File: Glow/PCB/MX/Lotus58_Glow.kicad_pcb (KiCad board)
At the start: 2 copper layers, 139.1 x 107.7 mm, 122 parts, among them J1 PJ-320A, P4 OLED, SW1 Kailh hotswap MX socket, SW10 Kailh hotswap MX socket, SW11 Kailh hotswap MX socket, SW12 Kailh hotswap MX socket, SW13 Kailh hotswap MX socket, SW14 Kailh hotswap MX socket, SW15 Kailh hotswap MX socket, SW16 Kailh hotswap MX socket, SW17 Kailh hotswap MX socket, SW18 Kailh hotswap MX socket, SW19 Kailh hotswap MX socket, SW2 Kailh hotswap MX socket, SW20 Kailh hotswap MX socket, SW21 Kailh hotswap MX socket, SW22 Kailh hotswap MX socket, SW23 Kailh hotswap MX socket, SW24 Kailh hotswap MX socket, SW25 Kailh hotswap MX socket, SW26 Kailh hotswap MX socket, SW27 Kailh hotswap MX socket, SW28 Kailh hotswap MX socket, SW29 Kailh hotswap MX socket, SW3 Kailh hotswap MX socket, SW30 Rotary_Encoder_Switch, SW31 Rotary_Encoder_Switch, SW4 Kailh hotswap MX socket, SW5 Kailh hotswap MX socket, SW6 Kailh hotswap MX socket, SW7 Kailh hotswap MX socket, SW8 Kailh hotswap MX socket, SW9 Kailh hotswap MX socket, U1 ProMicro

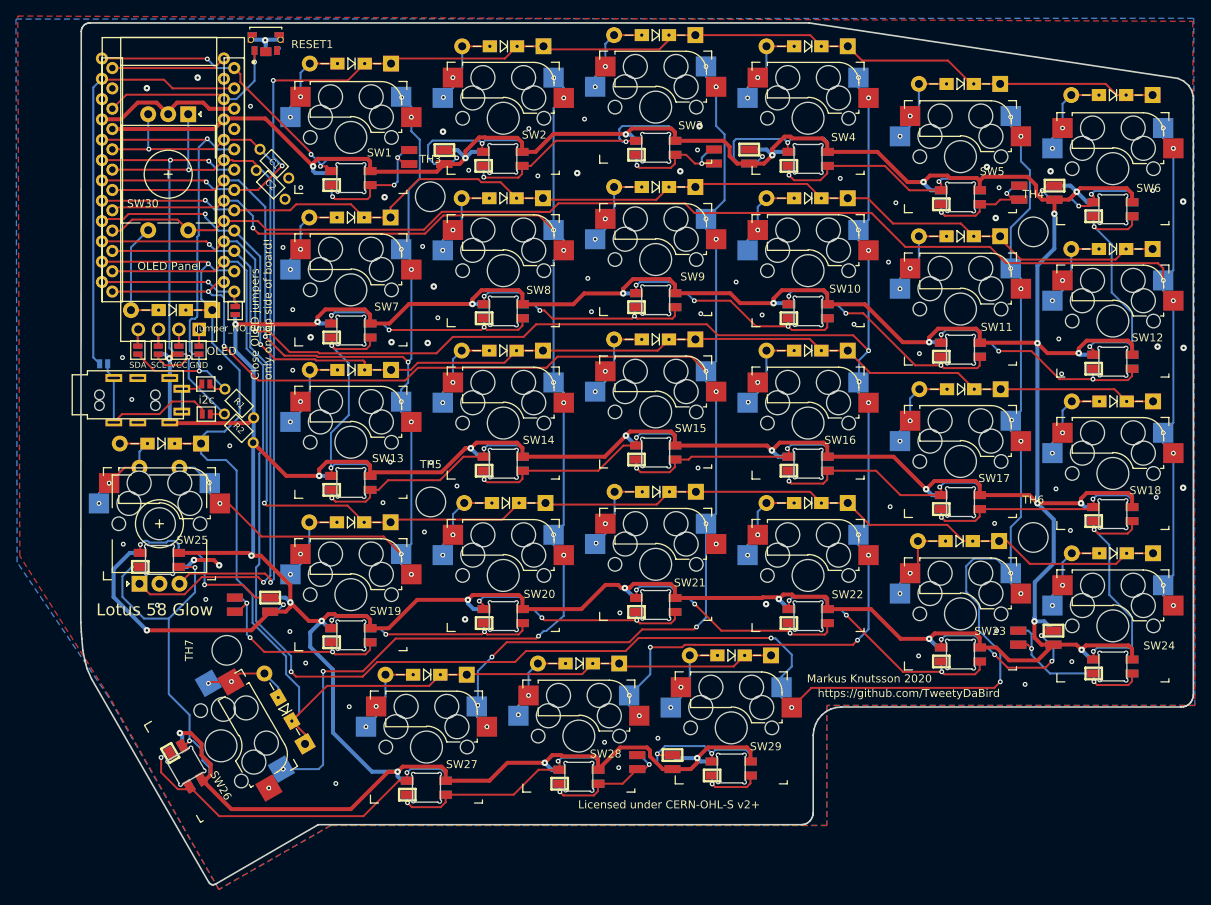
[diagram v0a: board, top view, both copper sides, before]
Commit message: Minor changes to silkscreen
- Added missing lables for jumpers
- Removed labels for holes(?)
- Corrected marker for RGB LED's
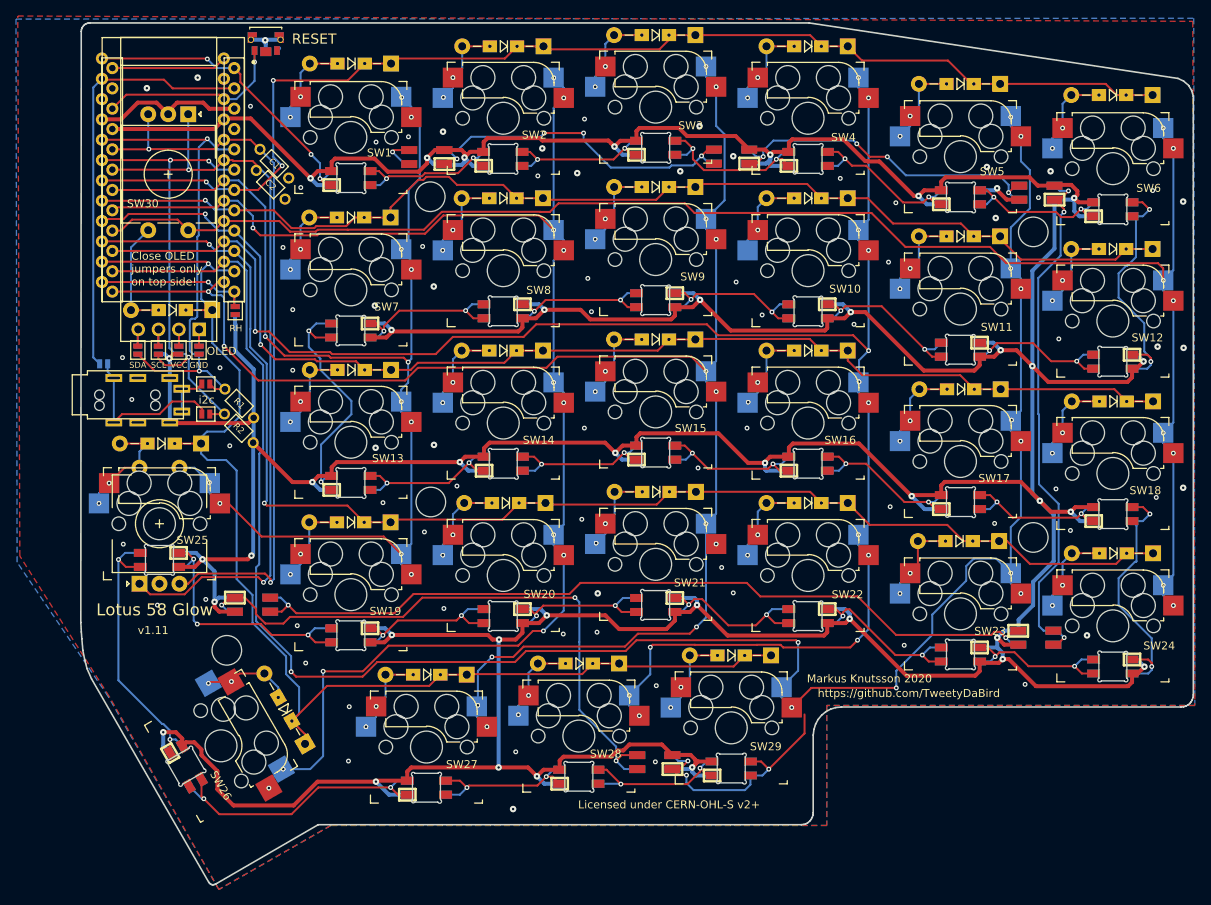
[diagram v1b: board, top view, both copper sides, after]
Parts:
- JP12: value Jumper_NO_Small -> LH
- JP13: value Jumper_NO_Small -> RH
- L1, L10, L11, L12, L13, L14, L15, L16, L17, L18, L19, L2, L20, L21, L22, L23, L24, L25, L26, L27, L28, L29, L3, L4, L5, L6, L7, L8, L9: footprint Keyboard Library:SK6812MINI_Midmount_Reversible -> Keyboard Library:SK6812MINI_Midmount_Reversible_v2
- L30: renamed from L31; footprint Keyboard Library:SK6812MINI_Reversible -> Keyboard Library:SK6812MINI_Doublesided
- L31: renamed from L32; footprint Keyboard Library:SK6812MINI_Reversible -> Keyboard Library:SK6812MINI_Doublesided
- L32: renamed from L30; footprint Keyboard Library:SK6812MINI_Reversible -> Keyboard Library:SK6812MINI_Doublesided
- L33, L34, L35: footprint Keyboard Library:SK6812MINI_Reversible -> Keyboard Library:SK6812MINI_Doublesided
- RESET1: value EVP-AKE31A -> RESET
- moved JP9 0.06 mm to (96.3, 84.6)
- turned L10 to 180 degrees
- turned L11 to 180 degrees
- turned L12 to 180 degrees
- turned L19 to 180 degrees
- turned L2 to 0 degrees
- turned L20 to 180 degrees
- turned L21 to 180 degrees
- turned L22 to 180 degrees
- turned L23 to 180 degrees
- turned L24 to 180 degrees
- turned L25 to 180 degrees
- turned L31 to 180 degrees
- turned L32 to 180 degrees
- turned L7 to 180 degrees
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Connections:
- L1 pad 1: GND -> Net-(L1-Pad1)
- L1 pad 2: LED -> GND
- L1 pad 3: VCC -> LED
- L1 pad 4: Net-(L1-Pad4) -> VCC
- L10 pad 1: GND -> Net-(L10-Pad1)
- L10 pad 2: Net-(L10-Pad2) -> GND
- L10 pad 3: VCC -> Net-(L10-Pad3)
- L10 pad 4: Net-(L10-Pad4) -> VCC
- L11 pad 1: GND -> Net-(L10-Pad3)
- L11 pad 2: Net-(L11-Pad2) -> GND
- L11 pad 3: VCC -> Net-(L11-Pad3)
- L11 pad 4: Net-(L10-Pad2) -> VCC
- L12 pad 1: GND -> Net-(L11-Pad3)
- L12 pad 2: Net-(L12-Pad2) -> GND
- L12 pad 3: VCC -> Net-(L12-Pad3)
- L12 pad 4: Net-(L11-Pad2) -> VCC
- L13 pad 1: GND -> Net-(L13-Pad1)
- L13 pad 2: Net-(L13-Pad2) -> GND
- L13 pad 3: VCC -> Net-(L13-Pad3)
- L13 pad 4: Net-(L13-Pad4) -> VCC
- L14 pad 1: GND -> Net-(L14-Pad1)
- L14 pad 2: Net-(L13-Pad4) -> GND
- L14 pad 3: VCC -> Net-(L13-Pad1)
- L14 pad 4: Net-(L14-Pad4) -> VCC
- L15 pad 1: GND -> Net-(L15-Pad1)
- L15 pad 2: Net-(L14-Pad4) -> GND
- L15 pad 3: VCC -> Net-(L14-Pad1)
- L15 pad 4: Net-(L15-Pad4) -> VCC
- L16 pad 1: GND -> Net-(L16-Pad1)
- L16 pad 2: Net-(L15-Pad4) -> GND
- L16 pad 3: VCC -> Net-(L15-Pad1)
- L16 pad 4: Net-(L16-Pad4) -> VCC
- L17 pad 1: GND -> Net-(L17-Pad1)
- L17 pad 2: Net-(L16-Pad4) -> GND
- L17 pad 3: VCC -> Net-(L16-Pad1)
- L17 pad 4: Net-(L17-Pad4) -> VCC
- L18 pad 1: GND -> Net-(L18-Pad1)
- L18 pad 2: Net-(L17-Pad4) -> GND
- L18 pad 3: VCC -> Net-(L17-Pad1)
- L18 pad 4: Net-(L18-Pad4) -> VCC
- L19 pad 1: GND -> Net-(L19-Pad1)
- L19 pad 2: Net-(L19-Pad2) -> GND
- L19 pad 3: VCC -> Net-(L19-Pad3)
- L19 pad 4: Net-(L19-Pad4) -> VCC
- L2 pad 1: GND -> Net-(L2-Pad1)
- L2 pad 2: Net-(L2-Pad2) -> GND
- L2 pad 3: VCC -> Net-(L1-Pad1)
- L2 pad 4: Net-(L2-Pad4) -> VCC
- L20 pad 1: GND -> Net-(L19-Pad3)
- L20 pad 2: Net-(L20-Pad2) -> GND
- L20 pad 3: VCC -> Net-(L20-Pad3)
- L20 pad 4: Net-(L19-Pad2) -> VCC
- L21 pad 1: GND -> Net-(L20-Pad3)
- L21 pad 2: Net-(L21-Pad2) -> GND
- L21 pad 3: VCC -> Net-(L21-Pad3)
- L21 pad 4: Net-(L20-Pad2) -> VCC
- L22 pad 1: GND -> Net-(L21-Pad3)
- L22 pad 2: Net-(L22-Pad2) -> GND
- L22 pad 3: VCC -> Net-(L22-Pad3)
- L22 pad 4: Net-(L21-Pad2) -> VCC
- L23 pad 1: GND -> Net-(L22-Pad3)
- L23 pad 2: Net-(L23-Pad2) -> GND
- L23 pad 3: VCC -> Net-(L23-Pad3)
- L23 pad 4: Net-(L22-Pad2) -> VCC
- L24 pad 1: GND -> Net-(L23-Pad3)
- L24 pad 2: Net-(L18-Pad4) -> GND
- L24 pad 3: VCC -> Net-(L18-Pad1)
- L24 pad 4: Net-(L24-Pad4) -> VCC
- L25 pad 1: GND -> Net-(L25-Pad1)
- L25 pad 2: Net-(L25-Pad2) -> GND
- L25 pad 3: VCC -> Net-(L19-Pad1)
- L25 pad 4: Net-(L25-Pad4) -> VCC
- L26 pad 1: GND -> Net-(L26-Pad1)
- L26 pad 2: Net-(L25-Pad4) -> GND
- L26 pad 3: VCC -> Net-(L25-Pad1)
- L26 pad 4: Net-(L26-Pad4) -> VCC
- L27 pad 1: GND -> Net-(L27-Pad1)
- L27 pad 2: Net-(L26-Pad4) -> GND
- L27 pad 3: VCC -> Net-(L26-Pad1)
- L27 pad 4: Net-(L27-Pad4) -> VCC
- L28 pad 1: GND -> Net-(L28-Pad1)
- L28 pad 2: Net-(L27-Pad4) -> GND
- L28 pad 3: VCC -> Net-(L27-Pad1)
- L28 pad 4: Net-(L28-Pad4) -> VCC
- L29 pad 1: GND -> Net-(L29-Pad1)
- L29 pad 2: Net-(L29-Pad2) -> GND
- L29 pad 3: VCC -> Net-(L28-Pad1)
- L29 pad 4: Net-(L29-Pad4) -> VCC
- L3 pad 1: GND -> Net-(L3-Pad1)
- L3 pad 2: Net-(L2-Pad4) -> GND
- L3 pad 3: VCC -> Net-(L2-Pad1)
- L3 pad 4: Net-(L3-Pad4) -> VCC
- L30 pad 1: GND -> Net-(L30-Pad1)
- L30 pad 2: Net-(L28-Pad4) -> GND
- L30 pad 3: VCC -> Net-(L29-Pad1)
- L30 pad 4: Net-(L29-Pad2) -> VCC
- L31 pad 1: GND -> Net-(L31-Pad1)
- L31 pad 2: Net-(L19-Pad4) -> GND
- L31 pad 3: VCC -> Net-(L30-Pad1)
- L31 pad 4: Net-(L25-Pad2) -> VCC
- L32 pad 1: GND -> Net-(L32-Pad1)
- L32 pad 2: Net-(L24-Pad4) -> GND
- L32 pad 3: VCC -> Net-(L31-Pad1)
- L32 pad 4: Net-(L23-Pad2) -> VCC
- L33 pad 1: GND -> Net-(L33-Pad1)
- L33 pad 2: Net-(L33-Pad2) -> GND
- L33 pad 3: VCC -> Net-(L32-Pad1)
- L33 pad 4: Net-(L33-Pad4) -> VCC
- L34 pad 1: GND -> Net-(L34-Pad1)
- L34 pad 2: Net-(L3-Pad4) -> GND
- L34 pad 3: VCC -> Net-(L33-Pad1)
- L34 pad 4: Net-(L34-Pad4) -> VCC
- L35 pad 1: GND -> Net-(L35-Pad1)
- L35 pad 2: Net-(L1-Pad4) -> GND
- L35 pad 3: VCC -> Net-(L34-Pad1)
- L35 pad 4: Net-(L2-Pad2) -> VCC
- L4 pad 1: GND -> Net-(L4-Pad1)
- L4 pad 2: Net-(L34-Pad4) -> GND
- L4 pad 3: VCC -> Net-(L3-Pad1)
- L4 pad 4: Net-(L4-Pad4) -> VCC
- L5 pad 1: GND -> Net-(L5-Pad1)
- L5 pad 2: Net-(L4-Pad4) -> GND
- L5 pad 3: VCC -> Net-(L4-Pad1)
- L5 pad 4: Net-(L33-Pad2) -> VCC
- L6 pad 1: GND -> Net-(L12-Pad3)
- L6 pad 2: Net-(L33-Pad4) -> GND
- L6 pad 3: VCC -> Net-(L5-Pad1)
- L6 pad 4: Net-(L12-Pad2) -> VCC
- L7 pad 1: GND -> Net-(L13-Pad3)
- L7 pad 2: Net-(L7-Pad2) -> GND
- L7 pad 3: VCC -> Net-(L7-Pad3)
- L7 pad 4: Net-(L13-Pad2) -> VCC
- L8 pad 1: GND -> Net-(L7-Pad3)
- L8 pad 2: Net-(L8-Pad2) -> GND
- L8 pad 3: VCC -> Net-(L8-Pad3)
- L8 pad 4: Net-(L7-Pad2) -> VCC
- L9 pad 1: GND -> Net-(L8-Pad3)
- L9 pad 2: Net-(L10-Pad4) -> GND
- L9 pad 3: VCC -> Net-(L10-Pad1)
- L9 pad 4: Net-(L8-Pad2) -> VCC
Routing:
- net Net-(L31-Pad1): track 0.00 -> 103.9 mm, vias 0 -> 2
- net Net-(L30-Pad1): track 0.00 -> 78.2 mm, vias 0 -> 3
- net Net-(L32-Pad1): track 0.00 -> 66.9 mm, vias 0 -> 3
- net VCC: track 891.5 -> 840.8 mm, vias 37 -> 38
- net Net-(L25-Pad4): track 46.4 -> 0.00 mm, vias 2 -> 0
- net Net-(L26-Pad4): track 45.6 -> 0.00 mm, vias 2 -> 0
- net Net-(L34-Pad1): track 0.00 -> 43.7 mm, vias 0 -> 4
- net Net-(L33-Pad1): track 0.00 -> 42.8 mm, vias 0 -> 4
- net Net-(L26-Pad1): track 0.00 -> 35.4 mm, vias 0 -> 2
- net Net-(L25-Pad1): track 0.00 -> 35.0 mm, vias 0 -> 2
- net Net-(L19-Pad1): track 0.00 -> 33.8 mm, vias 0 -> 3
- net Net-(L2-Pad4): track 33.7 -> 0.00 mm, vias 2 -> 0
- net Net-(L12-Pad2): track 33.4 -> 0.00 mm, vias 2 -> 0
- net Net-(L13-Pad3): track 0.00 -> 32.5 mm, vias 0 -> 2
- net Net-(L18-Pad1): track 0.00 -> 32.5 mm, vias 0 -> 2
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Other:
- board text added: "Close OLED jumpers only on top side!"
- board text added: "v1.11"
- board text removed: "Close OLED jumpers only on top side of board!"

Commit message: nothing
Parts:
- moved JP9 14.7 mm to (83.2, 77.8), turned to 270 degrees
- moved JP10 11.5 mm to (85.1, 77.8), turned to 90 degrees
- moved JP11 0.58 mm to (83.2, 77.8), turned to 90 degrees
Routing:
- net Net-(J1-PadR2): track 20.8 -> 10.4 mm
- net Net-(L29-Pad1): track 31.4 -> 22.7 mm
- net SCL: track 59.3 -> 66.8 mm, vias 3 -> 5
- net Net-(J1-PadS): track 5.59 -> 13.1 mm
- net DATA: track 53.4 -> 52.7 mm
- net SDA: track 63.1 -> 63.7 mm
- net GND: vias 78 -> 76
